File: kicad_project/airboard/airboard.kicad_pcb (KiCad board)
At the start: 2 copper layers, 47 x 33 mm, 0 parts

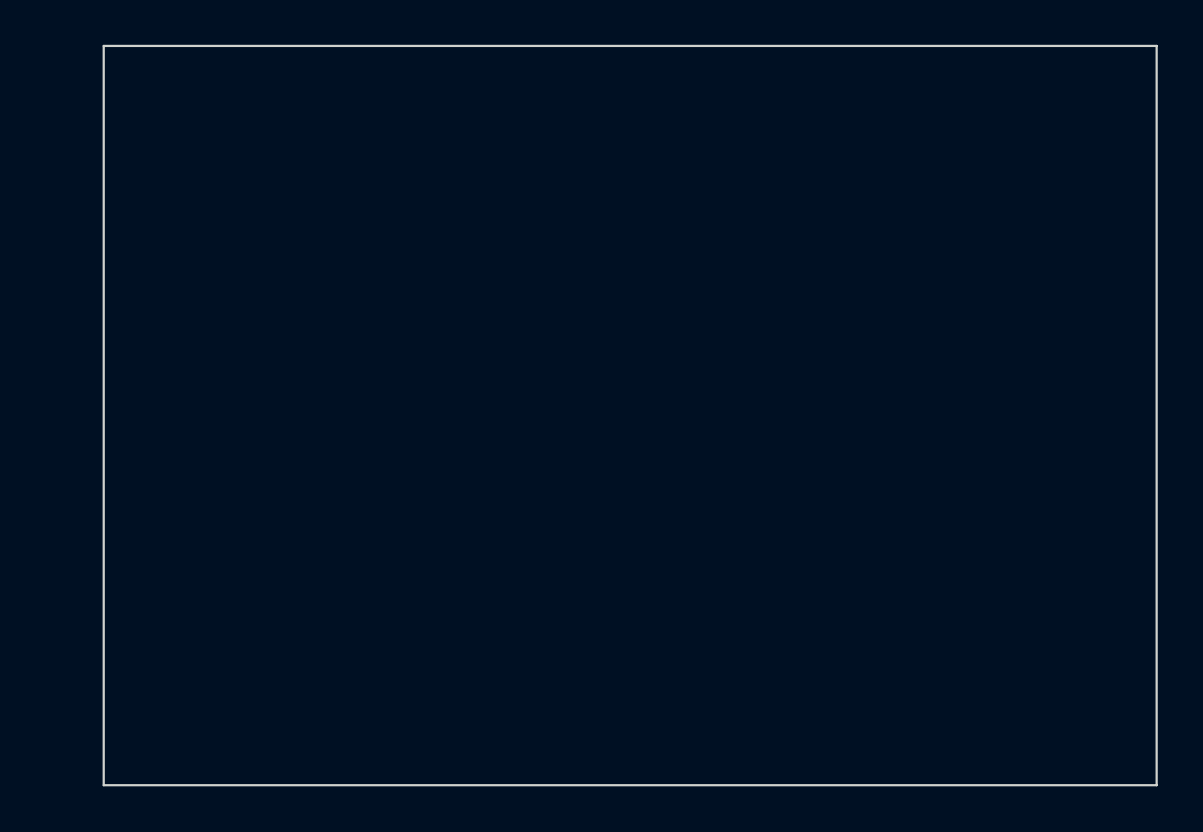
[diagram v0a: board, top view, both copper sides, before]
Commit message: feat(kicad_project): add new libraries and update symbol and footprint tables
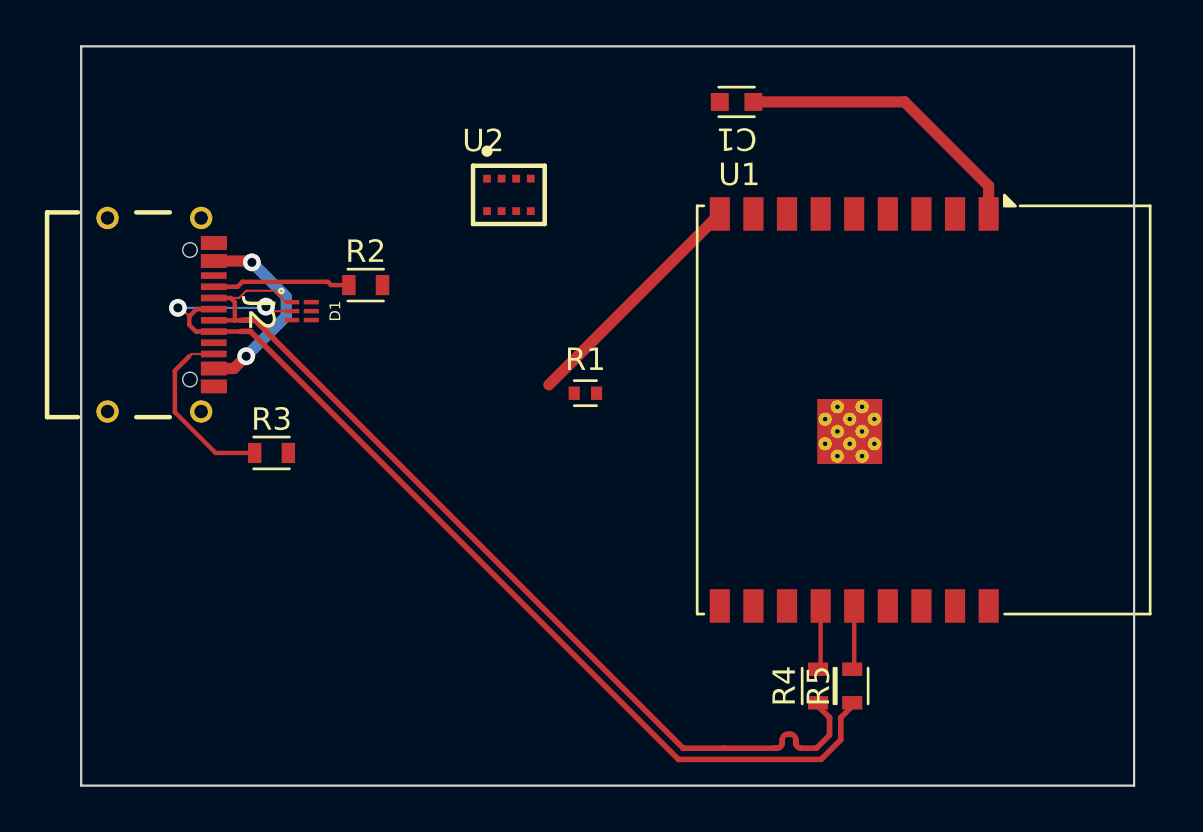
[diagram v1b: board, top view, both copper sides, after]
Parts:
- added C1: 0603_Fl0.35_R_885012106031, Capacitor_SMD_Wurth:C_Wurth_WCAP-CSGP-0603_Fl0.35_R, F.Cu at (108.2, 66.5)
- added D1: WE-TVS-SS_DFN1210-6L_824012823, WE-TVS-SS_DFN1210-6L_824012823:WE-TVS_DFN1210-6L, F.Cu at (88.8, 75.8)
- added J2: USB_C_Receptacle_USB2.0_14P, Eagle_WR-USB (rev25c):629722000214, F.Cu at (80.2, 76.0)
- added R1: 0402_560112110012, Resistor_SMD_Wurth:R_Wurth_WRIS-RSKS-0402, F.Cu at (101.5, 79.5)
- added R2: 0603_R_560112116017, Resistor_SMD_Wurth:R_Wurth_WRIS-RSKS-0603_R, F.Cu at (91.7, 74.7)
- added R3: 0603_R_560112116017, Resistor_SMD_Wurth:R_Wurth_WRIS-RSKS-0603_R, F.Cu at (87.5, 82.2)
- added R4: 0603_R_560112116043, Resistor_SMD_Wurth:R_Wurth_WRIS-RSKS-0603_R, F.Cu at (111.9, 92.6)
- added R5: 0603_R_560112116043, Resistor_SMD_Wurth:R_Wurth_WRIS-RSKS-0603_R, F.Cu at (113.4, 92.6)
- added U1: ESP32-C3-WROOM-02, RF_Module:ESP32-C3-WROOM-02, F.Cu at (113.5, 80.2)
- added U2: DPS368, DPS368:LGA8S145X65P2X4_200X250X110-V, F.Cu at (98.1, 70.6)
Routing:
- net /USB_DP: track 0.00 -> 46.8 mm, vias 0 -> 2
- net /USB_DN: track 0.00 -> 44.9 mm
- net +3.3V: track 0.00 -> 13.8 mm
- net GND: track 0.00 -> 11.1 mm
- net +5V: track 0.00 -> 8.96 mm, vias 0 -> 2
- net Net-(J2-CC2): track 0.00 -> 8.22 mm
- net Net-(J2-CC1): track 0.00 -> 6.18 mm
- net Net-(U1-IO18): track 0.00 -> 2.87 mm
- net Net-(U1-IO19): track 0.00 -> 2.86 mm
